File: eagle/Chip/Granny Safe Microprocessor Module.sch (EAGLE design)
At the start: 71 parts, among them IC1 MCP604SL, J1 3x4 Keypad, J4 213598-2, Q1 TRANS_NPN-MMBTA42, Q2 BT137-600E, Q3 TRANS_NPN-MMBTA42, Q4 TRANS_NPN-MMBTA42, U1 328P, U2 TRIAC_OPTOCOUPLER-MOC3063SM, U3 SFH6206, Y1 16MHz

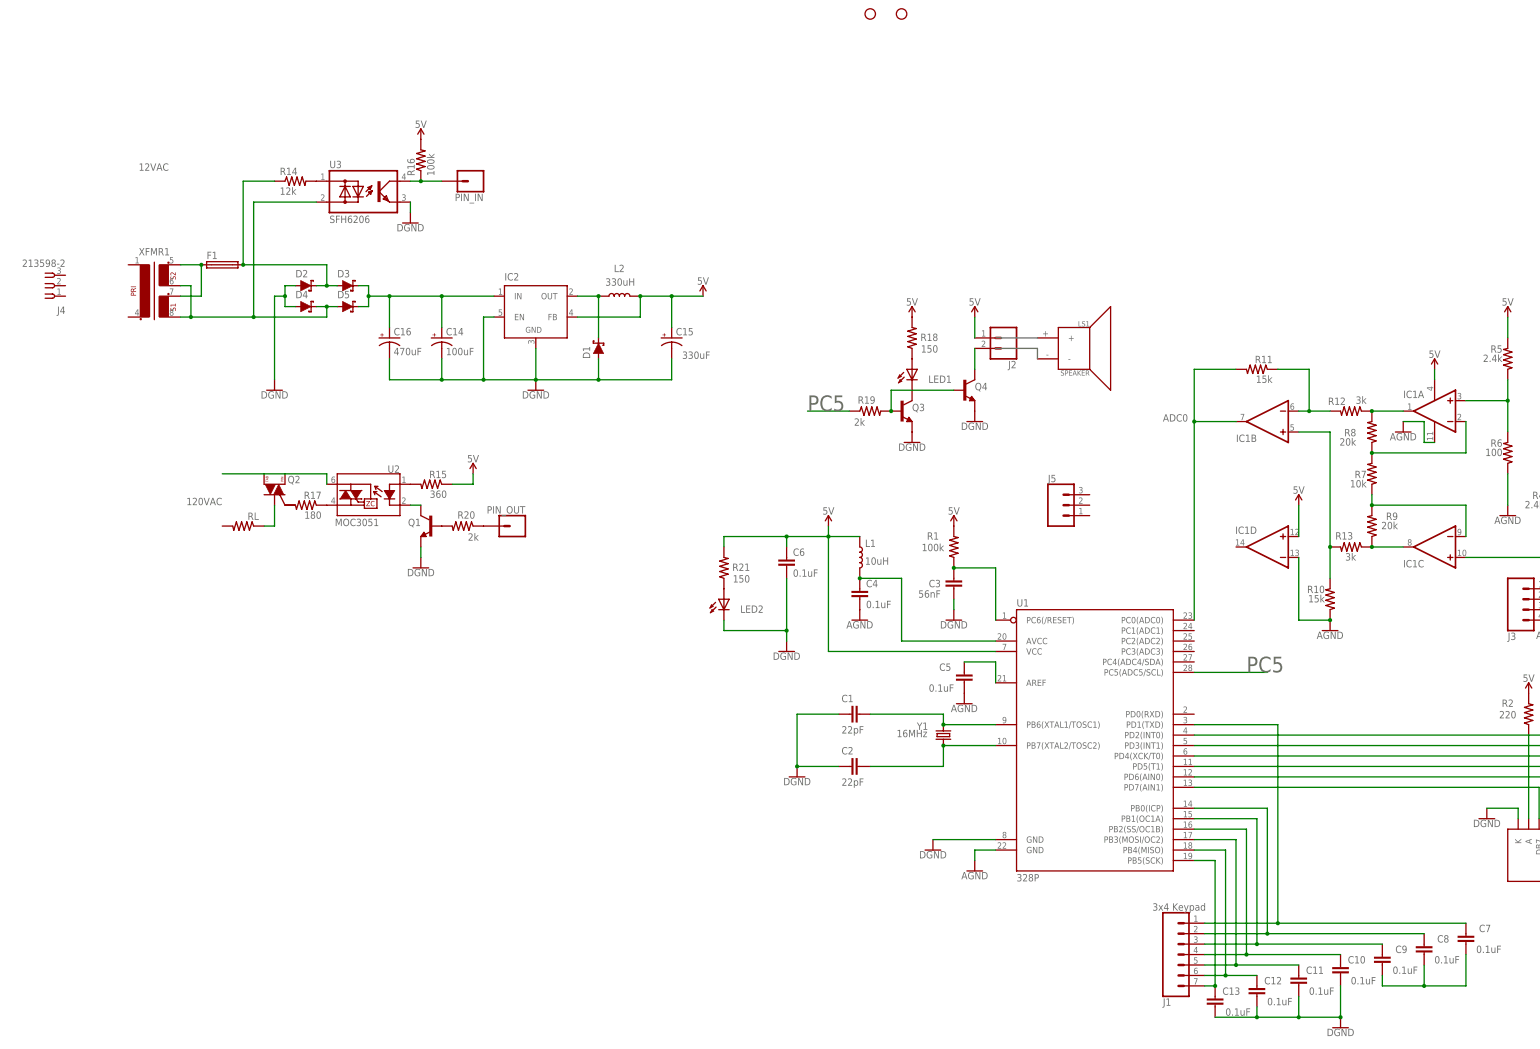
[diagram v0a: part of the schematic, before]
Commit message: Changed schematics and block diagram
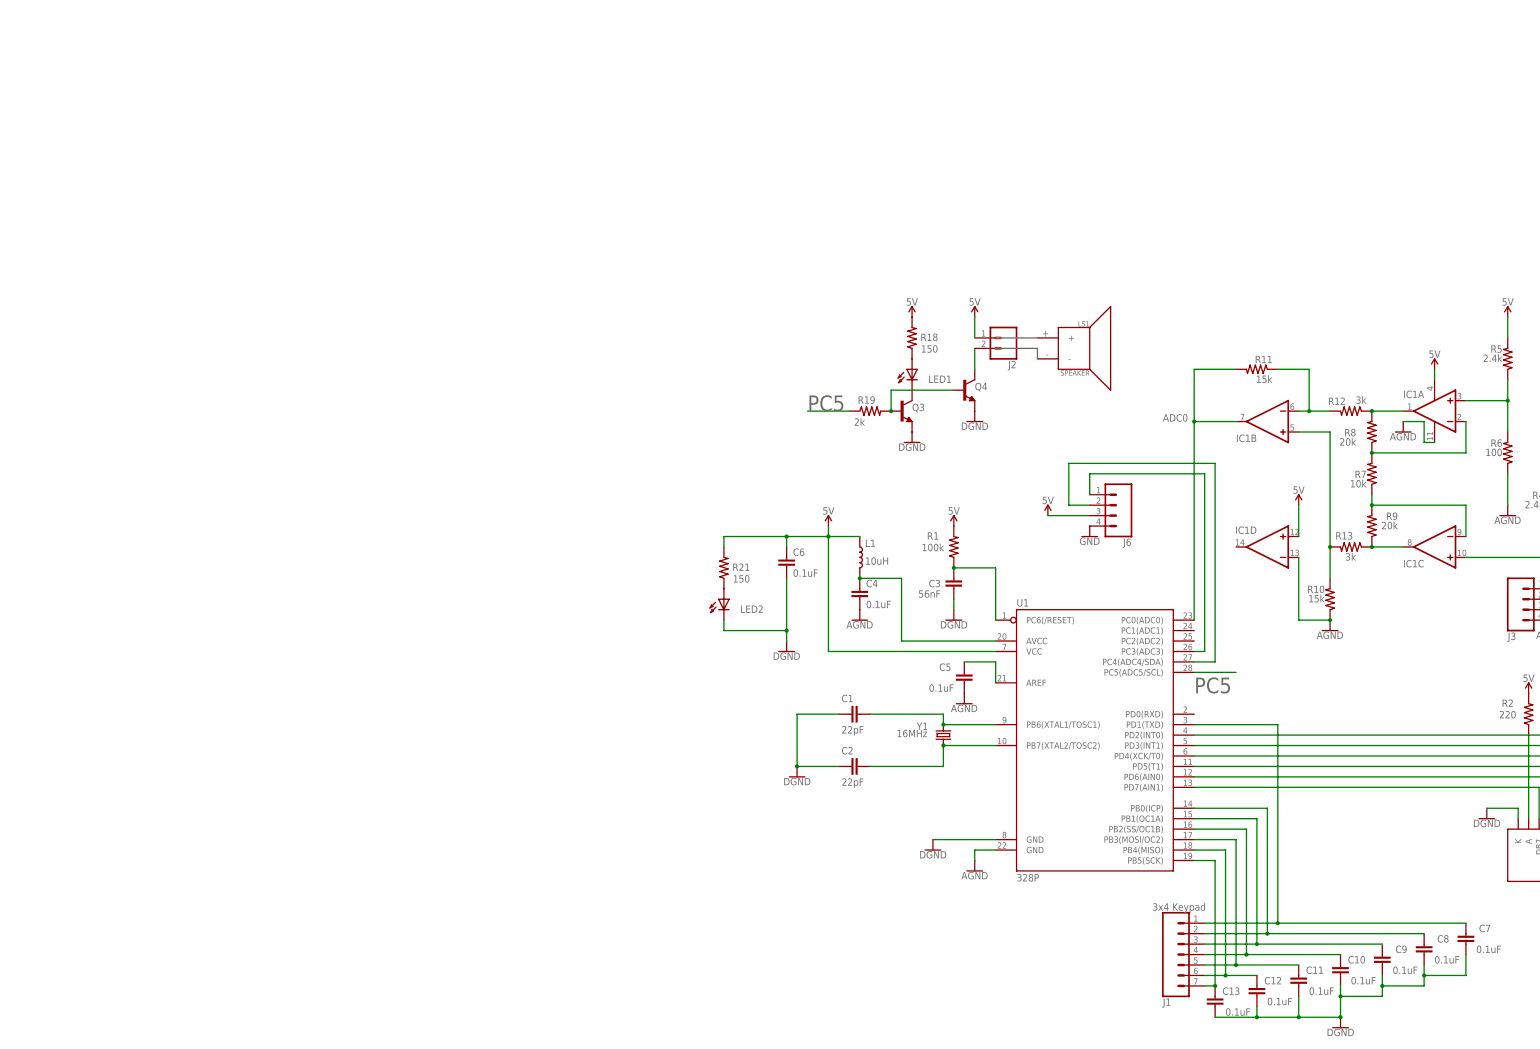
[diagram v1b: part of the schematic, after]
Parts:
- removed C14: 100uF, SparkFun-Capacitors:100UF-POLAR-RADIAL-2.5MM-25V-20%
- removed C15: 47UF-POLAR-PANASONIC_D-50V-20%, SparkFun-Capacitors:47UF-POLAR-PANASONIC_D-50V-20%
- removed C16: 470uF, SparkFun-Capacitors:47UF-POLAR-PANASONIC_D-35V-20%
- removed D1, D2, D3, D4, D5: DIODE-SCHOTTKY-B340A, SparkFun-DiscreteSemi:DIODE-SCHOTTKY-B340A
- removed F1: (no value), fuse:TE5
- removed H10, H11: STAND-OFF, SparkFun-Hardware:STAND-OFF
- removed IC2: (no value), linear:LM2596TH
- removed J4: 213598-2, con-amp:213598-2
- removed J5: (no value), SparkFun-Connectors:CONN_03
- removed L2: 330uH, SparkFun-Coils:INDUCTOR-CR75-68UH
- removed PIN_IN, PIN_OUT: (no value), SparkFun-Connectors:CONN_01
- removed Q1: TRANS_NPN-MMBTA42, SparkFun-DiscreteSemi:TRANS_NPN-MMBTA42
- removed Q2: BT137-600E, SparkFun-DiscreteSemi:TRIAC-Z0103MN
- removed R14: 12k, adafruit:R-US_R0603
- removed R15: 360, adafruit:R-US_R0603
- removed R16: 100k, adafruit:R-US_R0603
- removed R17: 180, adafruit:R-US_R0603
- removed R20: 2k, adafruit:R-US_R0603
- removed RL: (no value), adafruit:R-US_R0603
- removed U2: TRIAC_OPTOCOUPLER-MOC3063SM, SparkFun-DiscreteSemi:TRIAC_OPTOCOUPLER-MOC3063SM
- removed U3: SFH6206, optocoupler:SFH6206
- removed XFMR1: EE20-2, ece:EE20-2
- added J6: (no value), SparkFun-Connectors:CONN_04
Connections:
- removed net N$29: R14.2, U3.AC1
- removed net N$30: PIN_IN.1, R16.1, U3.C
- removed net N$31: R15.2, U2.A
- removed net N$32: R17.1, U2.T2
- removed net N$33: C7.2, C8.2, C9.2
- removed net N$34: Q1.C, U2.K
- removed net N$35: Q1.B, R20.2
- removed net N$36: Q2.T2@1, Q2.T2@2, U2.T1
- removed net N$37: Q2.T1, RL.1
- removed net N$41: PIN_OUT.1, R20.1
- removed net N$46: D1.C, IC2.OUT, L2.1
- removed net N$47: D2.C, D3.A, F1.2, R14.1
- removed net N$49: F1.1, XFMR1.4, XFMR1.6
- removed net N$51: C14.+, C16.+, D3.C, D5.C, IC2.IN
- removed net N$52: D4.C, D5.A, U3.AC2, XFMR1.3, XFMR1.5
- new net N$48: J6.2, U1.PC4(ADC4/SDA)
- new net N$50: J6.1, U1.PC3(ADC3)
- net 5V: now also J6.3; no longer C15.+, IC2.FB, L2.2, R15.1, R16.2
- net GND: now also C7.2, C8.2, C9.2, J6.4; no longer C14.-, C15.-, C16.-, D1.A, D2.A, D4.A, IC2.EN, IC2.GND, Q1.E, U3.E
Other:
- note removed: "120VAC"
- note removed: "12VAC"
- note removed: "330uF"
- note removed: "MOC3051"
